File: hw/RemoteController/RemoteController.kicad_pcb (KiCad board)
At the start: 2 copper layers, 15 parts, among them U1 nRF52810-QCxx, U2 TPS562200, Y4 13.56 MHz

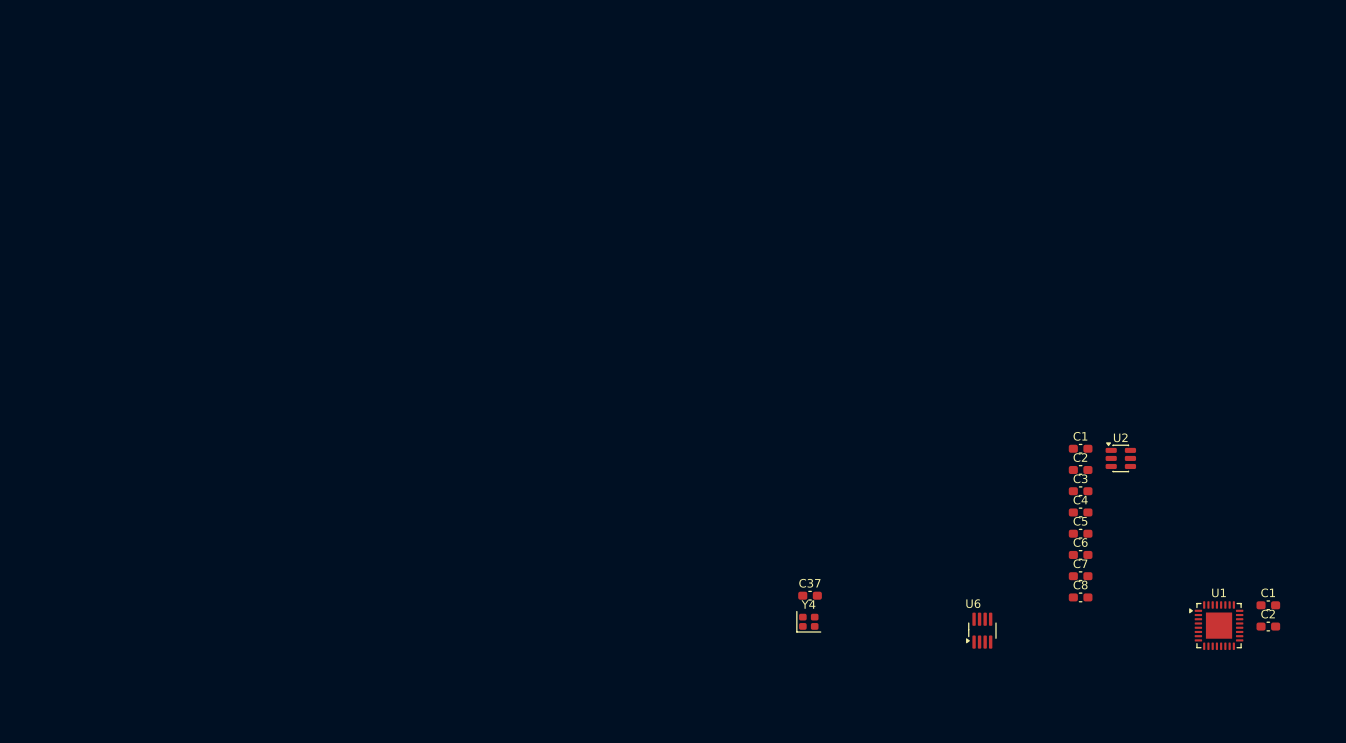
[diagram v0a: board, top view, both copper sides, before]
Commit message: remote_ctrl: add radio and change mcu
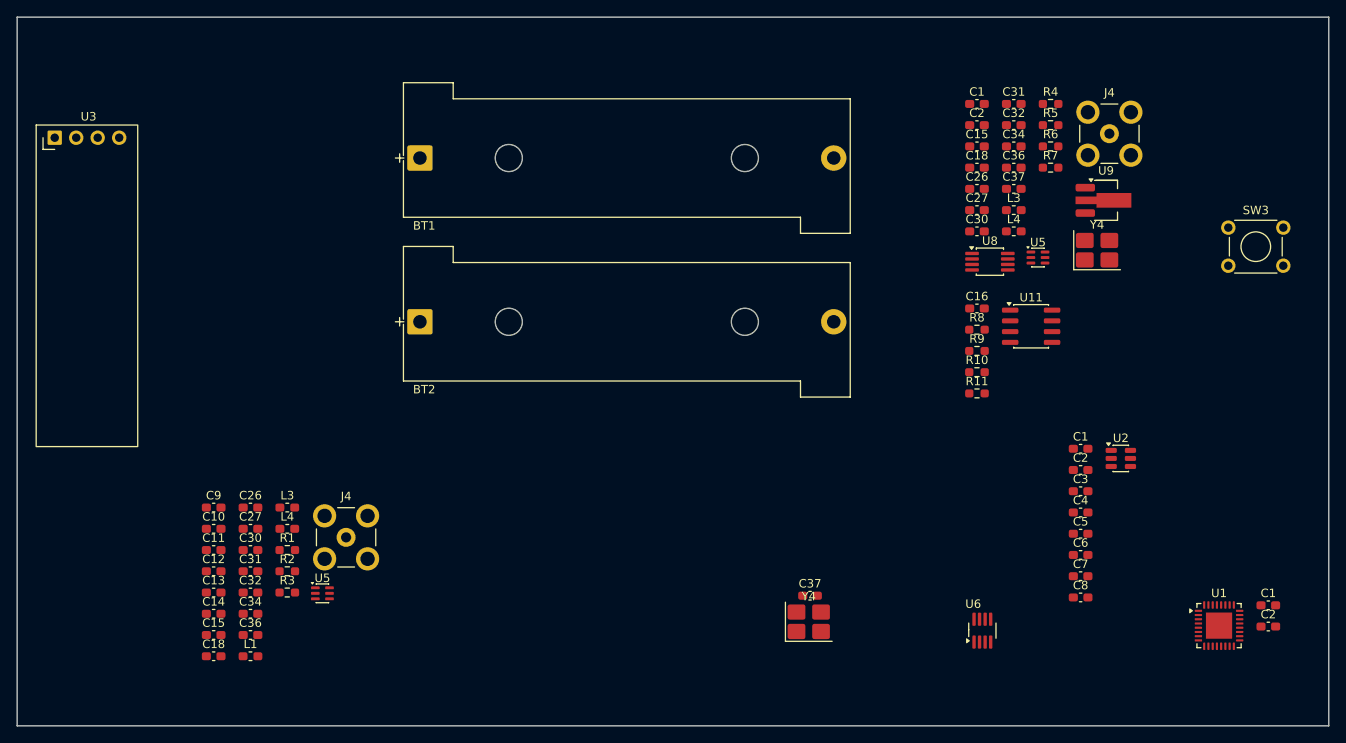
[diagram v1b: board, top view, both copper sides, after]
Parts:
- added BT1: Battery_Cell, Battery:BatteryHolder_Bulgin_BX0034_1xAAA, F.Cu at (73.8, 34.4)
- added BT2: Battery_Cell, Battery:BatteryHolder_Bulgin_BX0034_1xAAA, F.Cu at (73.8, 53.8)
- added C1: C, Capacitor_SMD:C_0603_1608Metric_Pad1.08x0.95mm_HandSolder, F.Cu at (139.7, 28.0)
- added C10: 10U, Capacitor_SMD:C_0603_1608Metric_Pad1.08x0.95mm_HandSolder, F.Cu at (49.5, 78.2)
- added C11: 100N, Capacitor_SMD:C_0603_1608Metric_Pad1.08x0.95mm_HandSolder, F.Cu at (49.5, 80.7)
- added C12: 22U, Capacitor_SMD:C_0603_1608Metric_Pad1.08x0.95mm_HandSolder, F.Cu at (49.5, 83.2)
- added C13: 22U, Capacitor_SMD:C_0603_1608Metric_Pad1.08x0.95mm_HandSolder, F.Cu at (49.5, 85.7)
- added C14: 100N, Capacitor_SMD:C_0603_1608Metric_Pad1.08x0.95mm_HandSolder, F.Cu at (49.5, 88.3)
- added C15: 220P, Capacitor_SMD:C_0603_1608Metric_Pad1.08x0.95mm_HandSolder, F.Cu at (49.5, 90.8)
- added C15: 220P, Capacitor_SMD:C_0603_1608Metric_Pad1.08x0.95mm_HandSolder, F.Cu at (139.7, 33.0)
- added C16: 100N, Capacitor_SMD:C_0603_1608Metric_Pad1.08x0.95mm_HandSolder, F.Cu at (139.7, 52.2)
- added C18: 680P, Capacitor_SMD:C_0603_1608Metric_Pad1.08x0.95mm_HandSolder, F.Cu at (139.7, 35.5)
- added C18: 680P, Capacitor_SMD:C_0603_1608Metric_Pad1.08x0.95mm_HandSolder, F.Cu at (49.5, 93.3)
- added C2: C, Capacitor_SMD:C_0603_1608Metric_Pad1.08x0.95mm_HandSolder, F.Cu at (139.7, 30.5)
- added C26: 100N, Capacitor_SMD:C_0603_1608Metric_Pad1.08x0.95mm_HandSolder, F.Cu at (53.8, 75.7)
- added C26: 100N, Capacitor_SMD:C_0603_1608Metric_Pad1.08x0.95mm_HandSolder, F.Cu at (139.7, 38.0)
- added C27: 1000P, Capacitor_SMD:C_0603_1608Metric_Pad1.08x0.95mm_HandSolder, F.Cu at (53.8, 78.2)
- added C27: 1000P, Capacitor_SMD:C_0603_1608Metric_Pad1.08x0.95mm_HandSolder, F.Cu at (139.7, 40.6)
- added C30: 15P, Capacitor_SMD:C_0603_1608Metric_Pad1.08x0.95mm_HandSolder, F.Cu at (53.8, 80.7)
- added C30: 15P, Capacitor_SMD:C_0603_1608Metric_Pad1.08x0.95mm_HandSolder, F.Cu at (139.7, 43.1)
- added C31: 18P, Capacitor_SMD:C_0603_1608Metric_Pad1.08x0.95mm_HandSolder, F.Cu at (144.0, 28.0)
- added C31: 18P, Capacitor_SMD:C_0603_1608Metric_Pad1.08x0.95mm_HandSolder, F.Cu at (53.8, 83.2)
- added C32: 1000P, Capacitor_SMD:C_0603_1608Metric_Pad1.08x0.95mm_HandSolder, F.Cu at (53.8, 85.7)
- added C32: 1000P, Capacitor_SMD:C_0603_1608Metric_Pad1.08x0.95mm_HandSolder, F.Cu at (144.0, 30.5)
- added C34: 1000P, Capacitor_SMD:C_0603_1608Metric_Pad1.08x0.95mm_HandSolder, F.Cu at (53.8, 88.3)
- added C34: 1000P, Capacitor_SMD:C_0603_1608Metric_Pad1.08x0.95mm_HandSolder, F.Cu at (144.0, 33.0)
- added C36: 12P, Capacitor_SMD:C_0603_1608Metric_Pad1.08x0.95mm_HandSolder, F.Cu at (53.8, 90.8)
- added C36: 12P, Capacitor_SMD:C_0603_1608Metric_Pad1.08x0.95mm_HandSolder, F.Cu at (144.0, 35.5)
- added C37: 100N, Capacitor_SMD:C_0603_1608Metric_Pad1.08x0.95mm_HandSolder, F.Cu at (144.0, 38.0)
- added C9: 10U, Capacitor_SMD:C_0603_1608Metric_Pad1.08x0.95mm_HandSolder, F.Cu at (49.5, 75.7)
- added J4: BWSMA-KE-Z001, Connector_Coaxial:SMB_Jack_Vertical, F.Cu at (155.3, 31.5)
- added J4: BWSMA-KE-Z001, Connector_Coaxial:SMB_Jack_Vertical, F.Cu at (65.1, 79.2)
- added L1: 2U2, Inductor_SMD:L_0603_1608Metric_Pad1.05x0.95mm_HandSolder, F.Cu at (53.8, 93.3)
- added L3: 27N, Inductor_SMD:L_0603_1608Metric_Pad1.05x0.95mm_HandSolder, F.Cu at (58.2, 75.7)
- added L3: 27N, Inductor_SMD:L_0603_1608Metric_Pad1.05x0.95mm_HandSolder, F.Cu at (144.0, 40.6)
- added L4: VHF160808H18NJT, Inductor_SMD:L_0603_1608Metric_Pad1.05x0.95mm_HandSolder, F.Cu at (144.0, 43.1)
- added L4: VHF160808H18NJT, Inductor_SMD:L_0603_1608Metric_Pad1.05x0.95mm_HandSolder, F.Cu at (58.2, 78.2)
- added R1: 50K, Resistor_SMD:R_0603_1608Metric_Pad0.98x0.95mm_HandSolder, F.Cu at (58.2, 80.7)
- added R10: 0R, Resistor_SMD:R_0603_1608Metric_Pad0.98x0.95mm_HandSolder, F.Cu at (139.7, 59.7)
- added R11: 0R, Resistor_SMD:R_0603_1608Metric_Pad0.98x0.95mm_HandSolder, F.Cu at (139.7, 62.2)
- added R2: 10K, Resistor_SMD:R_0603_1608Metric_Pad0.98x0.95mm_HandSolder, F.Cu at (58.2, 83.2)
- added R3: 3K3, Resistor_SMD:R_0603_1608Metric_Pad0.98x0.95mm_HandSolder, F.Cu at (58.2, 85.7)
- added R4: 50R, Resistor_SMD:R_0603_1608Metric_Pad0.98x0.95mm_HandSolder, F.Cu at (148.4, 28.0)
- added R5: 91R, Resistor_SMD:R_0603_1608Metric_Pad0.98x0.95mm_HandSolder, F.Cu at (148.4, 30.5)
- added R6: 82R, Resistor_SMD:R_0603_1608Metric_Pad0.98x0.95mm_HandSolder, F.Cu at (148.4, 33.0)
- added R7: 91R, Resistor_SMD:R_0603_1608Metric_Pad0.98x0.95mm_HandSolder, F.Cu at (148.4, 35.5)
- added R8: 50K, Resistor_SMD:R_0603_1608Metric_Pad0.98x0.95mm_HandSolder, F.Cu at (139.7, 54.7)
- added R9: 50K, Resistor_SMD:R_0603_1608Metric_Pad0.98x0.95mm_HandSolder, F.Cu at (139.7, 57.2)
- added SW3: SW_Push, Button_Switch_THT:SW_TH_Tactile_Omron_B3F-106x, F.Cu at (169.4, 42.6)
- added U11: LM358, Package_SO:SOIC-8_3.9x4.9mm_P1.27mm, F.Cu at (146.1, 54.3)
- added U3: ER_OLEDM0.91_1x-I2C, Display:ER_OLEDM0.91_1x-I2C, F.Cu at (30.7, 32.0)
- added U5: XA17-G4K, Package_TO_SOT_SMD:SOT-363_SC-70-6, F.Cu at (62.3, 85.8)
- added U5: XA17-G4K, Package_TO_SOT_SMD:SOT-363_SC-70-6, F.Cu at (146.9, 46.2)
- added U8: AD8313xRM, Package_SO:MSOP-8_3x3mm_P0.65mm, F.Cu at (141.2, 46.6)
- added U9: GVA-63, Package_TO_SOT_SMD:SOT-89-3_Handsoldering, F.Cu at (154.9, 39.4)
- added Y4: 13.56 MHz, Crystal:Crystal_SMD_3225-4Pin_3.2x2.5mm_HandSoldering, F.Cu at (153.9, 45.3)
- C37: value 100 nF -> 100N
- Y4: footprint Crystal:Crystal_SMD_2016-4Pin_2.0x1.6mm -> Crystal:Crystal_SMD_3225-4Pin_3.2x2.5mm_HandSoldering
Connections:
- C37 pad 1: +3V3 -> +3V0
- C7 pad 1: +2V5 -> +3V0
- C8 pad 1: +2V5 -> +3V0
- U1 pad 10: unconnected-(U1-P0.12-Pad10) -> /OLED_SDA
- U1 pad 20: Net-(U1-VSS-Pad20) -> GND
- U1 pad 25: +2V5 -> +3V0
- U1 pad 29: Net-(U1-VSS-Pad20) -> GND
- U1 pad 32: +2V5 -> +3V0
- U1 pad 33: Net-(U1-VSS-Pad20) -> GND
- U1 pad 4: unconnected-(U1-P0.04/AIN2-Pad4) -> /BAT2_SAMPLE
- U1 pad 5: unconnected-(U1-P0.05/AIN3-Pad5) -> /BAT1_SAMPLE
- U1 pad 6: unconnected-(U1-P0.06-Pad6) -> /TXDATA
- U1 pad 7: unconnected-(U1-P0.09-Pad7) -> /TXCLK
- U1 pad 8: unconnected-(U1-P0.10-Pad8) -> /OLED_SCL
- U1 pad 9: +2V5 -> +3V0
- U2 pad 1: unconnected-(U2-GND-Pad1) -> GND
- U2 pad 2: unconnected-(U2-SW-Pad2) -> Net-(U2-SW)
- U2 pad 3: unconnected-(U2-VIN-Pad3) -> /VBAT2
- U2 pad 4: unconnected-(U2-VFB-Pad4) -> Net-(U2-VFB)
- U2 pad 5: unconnected-(U2-EN-Pad5) -> Net-(U2-EN)
- U2 pad 6: unconnected-(U2-VBST-Pad6) -> Net-(U2-VBST)
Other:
- board outline added: 155 x 83.8 mm
